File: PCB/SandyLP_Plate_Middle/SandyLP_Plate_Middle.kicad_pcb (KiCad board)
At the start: 2 copper layers, 113.1 x 58.7 mm, 8 parts

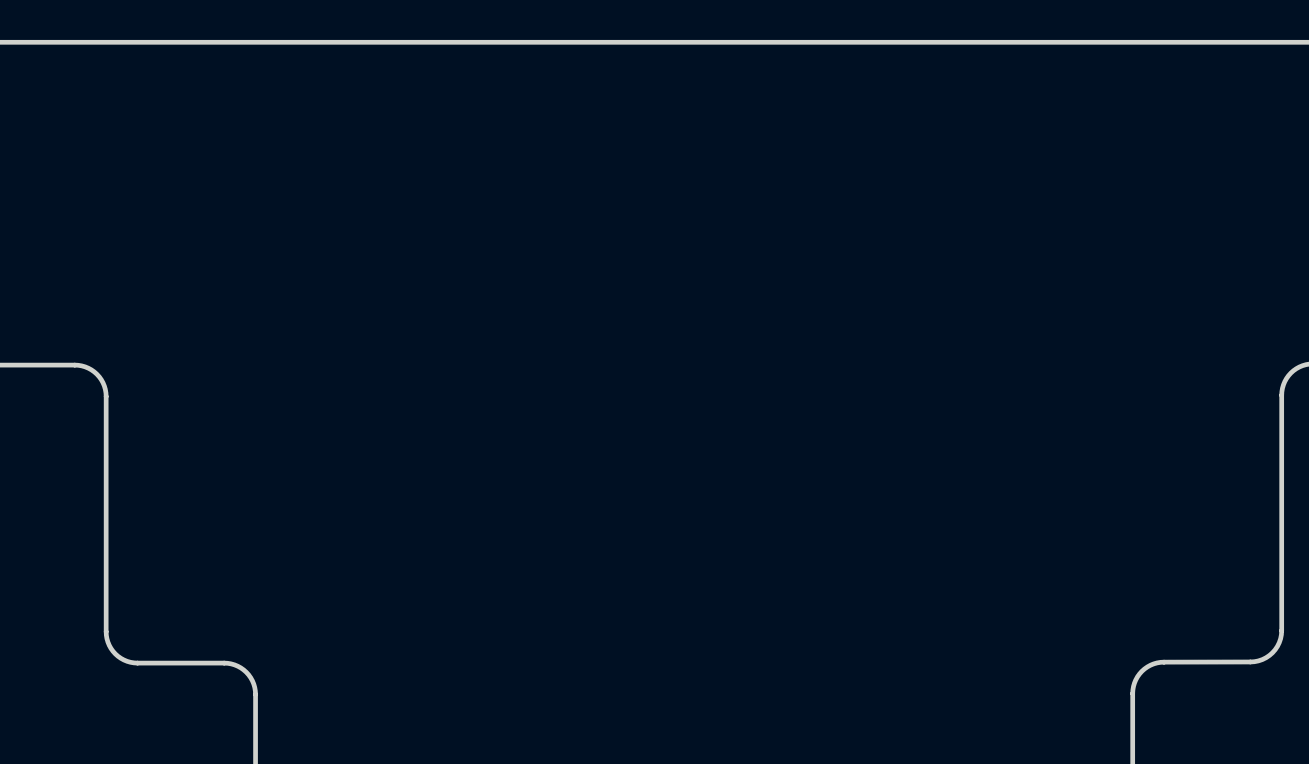
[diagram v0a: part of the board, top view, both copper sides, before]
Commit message: Top基板裏面のパーツ干渉を回避するため、穴を開けた。
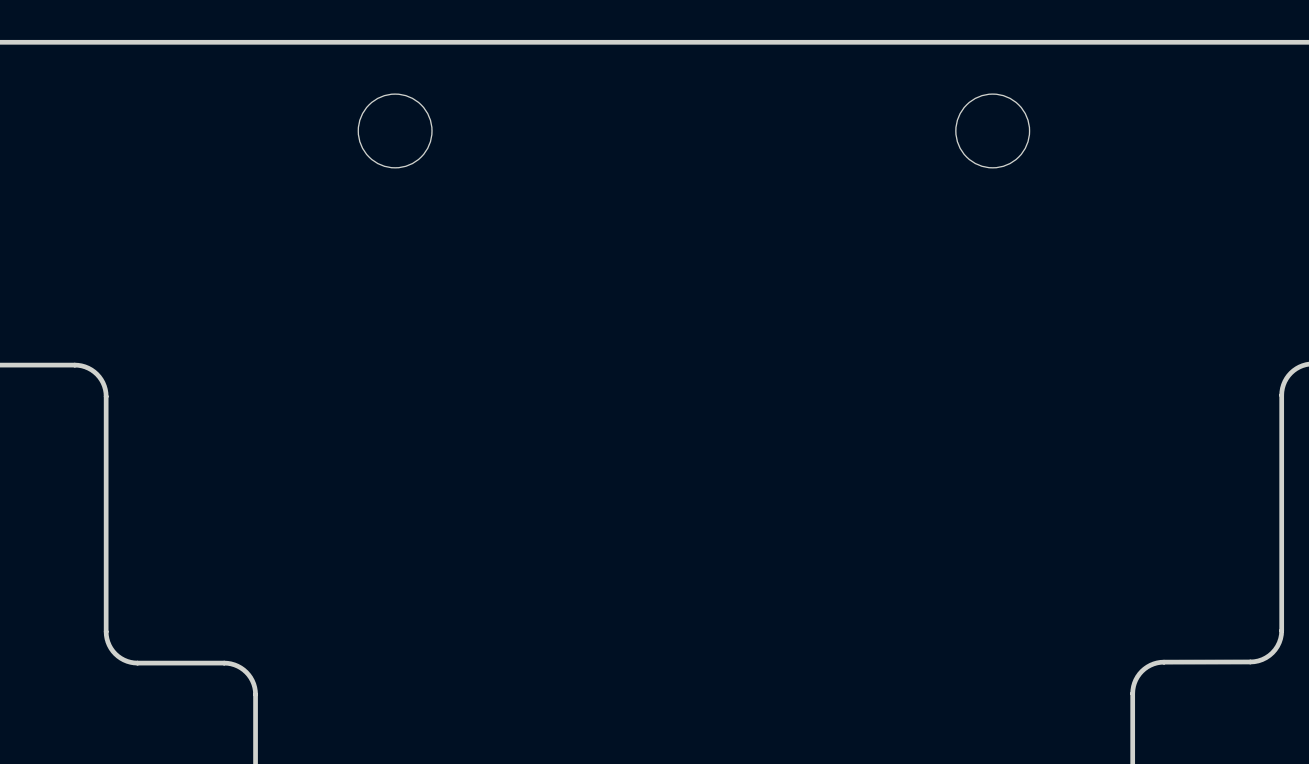
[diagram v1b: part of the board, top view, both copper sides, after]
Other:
- board text removed: "JLCJLCJLCJLC"

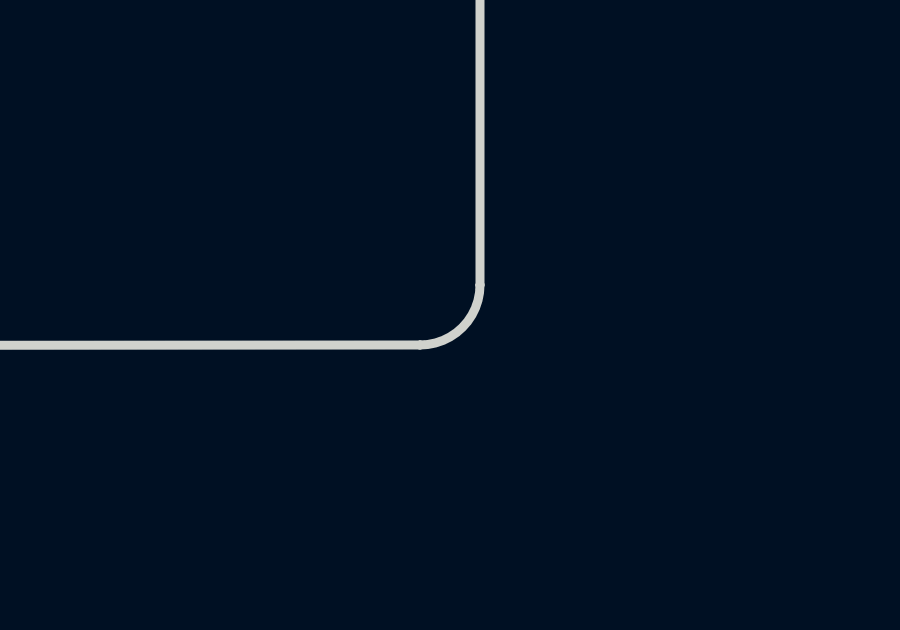
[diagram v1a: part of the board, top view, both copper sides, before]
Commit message: オプションが無料になったのでJLCのマーキングを削除。その他シルク位置調整。
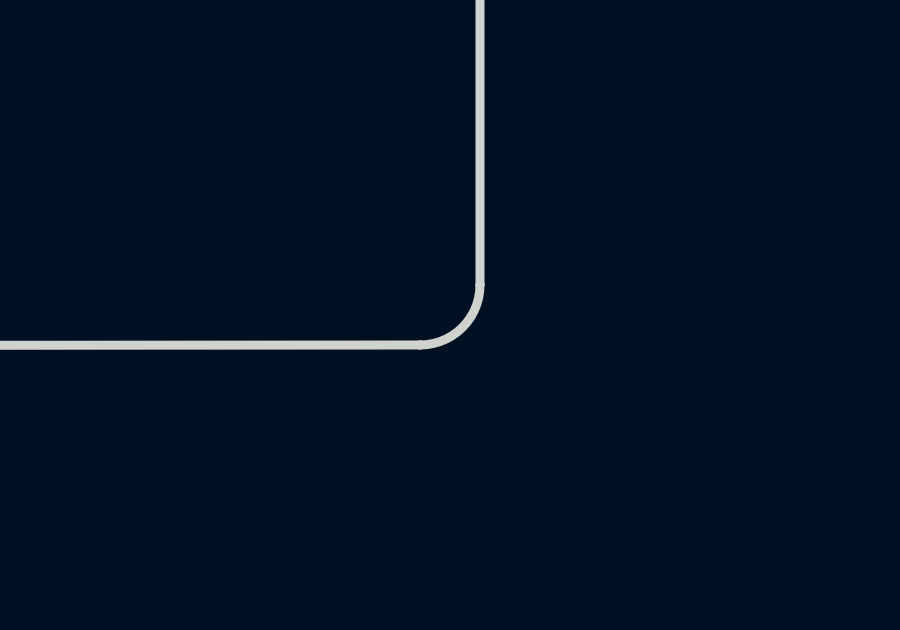
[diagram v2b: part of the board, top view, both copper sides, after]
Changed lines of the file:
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@@
 		(allow_soldermask_bridges_in_footprints no)
 		(aux_axis_origin 21.058435 21.05028)
-		(grid_origin 182.983435 40.10028)
+		(grid_origin 25.789685 37.623526)
 		(pcbplotparams
 			(layerselection 0x00310fc_ffffffff)
@@
 		(fp_arc
 			(start 137.7125 -2.628468)
-			(mid 137.126708 -1.21424)
+			(mid 137.126702 -1.214275)
 			(end 135.7125 -0.628468)
 			(stroke
@@
 		(fp_arc
 			(start 27.975 35.520746)
-			(mid 27.389203 36.934965)
+			(mid 27.389212 36.934959)
 			(end 25.975 37.520746)
 			(stroke
@@
 		(fp_arc
 			(start 56.555 -2.638468)
-			(mid 55.969202 -1.224275)
+			(mid 55.969208 -1.22424)
 			(end 54.555 -0.638468)
 			(stroke
